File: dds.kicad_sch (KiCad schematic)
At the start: 23 parts, among them J2 Conn_01x01_Pin, U4 AD8014ARZ, U6 AD9834, Y1 ASE-xxxMHz

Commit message: draf 1 for sims
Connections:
- net Signal renamed SIGNAL
- net reset renamed RESET
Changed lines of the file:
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@@
 		)
 	)
-	(global_label "Signal"
+	(label "MCLK"
+		(at 106.68 120.65 180)
+		(effects
+			(font
+				(size 1.27 1.27)
+			)
+			(justify right bottom)
+		)
+	)
+	(label "MCLK"
+		(at 168.91 77.47 0)
+		(effects
+			(font
+				(size 1.27 1.27)
+			)
+			(justify left bottom)
+		)
+	)
+	(hierarchical_label "FSYNC"
+		(shape input)
+		(at 106.68 105.41 180)
+		(effects
+			(font
+				(size 1.27 1.27)
+			)
+			(justify right)
+		)
+	)
+	(hierarchical_label "RESET"
+		(shape input)
+		(at 106.68 107.95 180)
+		(effects
+			(font
+				(size 1.27 1.27)
+			)
+			(justify right)
+		)
+	)
+	(hierarchical_label "SCLK"
+		(shape input)
+		(at 106.68 100.33 180)
+		(effects
+			(font
+				(size 1.27 1.27)
+			)
+			(justify right)
+		)
+	)
+	(hierarchical_label "SDATA"
+		(shape input)
+		(at 106.68 102.87 180)
+		(effects
+			(font
+				(size 1.27 1.27)
+			)
+			(justify right)
+		)
+	)
+	(hierarchical_label "SIGNAL"
 		(shape input)
 		(at 266.7 118.11 0)
-		(fields_autoplaced yes)
 		(effects
 			(font
@@
 			(justify left)
 		)
-		(property "Intersheetrefs" "${INTERSHEET_REFS}"
-			(at 275.6117 118.11 0)
-			(effects
-				(font
-					(size 1.27 1.27)
-				)
-				(justify left)
-				(hide yes)
-			)
-		)
 	)
-	(global_label "reset"
-		(shape input)
-		(at 106.68 107.95 180)
-		(fields_autoplaced yes)
-		(effects
-			(font
-				(size 1.27 1.27)
-			)
-			(justify right)
-		)
-		(property "Intersheetrefs" "${INTERSHEET_REFS}"
-			(at 98.9776 107.95 0)
-			(effects
-				(font
-					(size 1.27 1.27)
-				)
-				(justify right)
-				(hide yes)
-			)
-		)
-	)
-	(global_label "SDATA"
-		(shape input)
-		(at 106.68 102.87 180)
-		(fields_autoplaced yes)
-		(effects
-			(font
-				(size 1.27 1.27)
-			)
-			(justify right)
-		)
-		(property "Intersheetrefs" "${INTERSHEET_REFS}"
-			(at 98.0705 102.87 0)
-			(effects
-				(font
-					(size 1.27 1.27)
-				)
-				(justify right)
-				(hide yes)
-			)
-		)
-	)
-	(global_label "MCLK"
-		(shape input)
-		(at 168.91 77.47 0)
-		(fields_autoplaced yes)
-		(effects
-			(font
-				(size 1.27 1.27)
-			)
-			(justify left)
-		)
-		(property "Intersheetrefs" "${INTERSHEET_REFS}"
-			(at 176.9147 77.47 0)
-			(effects
-				(font
-					(size 1.27 1.27)
-				)
-				(justify left)
-				(hide yes)
-			)
-		)
-	)
-	(global_label "FSYNC"
-		(shape input)
-		(at 106.68 105.41 180)
-		(fields_autoplaced yes)
-		(effects
-			(font
-				(size 1.27 1.27)
-			)
-			(justify right)
-		)
-		(property "Intersheetrefs" "${INTERSHEET_REFS}"
-			(at 97.7076 105.41 0)
-			(effects
-				(font
-					(size 1.27 1.27)
-				)
-				(justify right)
-				(hide yes)
-			)
-		)
-	)
-	(global_label "SCLK"
-		(shape input)
-		(at 106.68 100.33 180)
-		(fields_autoplaced yes)
-		(effects
-			(font
-				(size 1.27 1.27)
-			)
-			(justify right)
-		)
-		(property "Intersheetrefs" "${INTERSHEET_REFS}"
-			(at 98.9172 100.33 0)
-			(effects
-				(font
-					(size 1.27 1.27)
-				)
-				(justify right)
-				(hide yes)
-			)
-		)
-	)
-	(global_label "MCLK"
-		(shape input)
-		(at 106.68 120.65 180)
-		(fields_autoplaced yes)
-		(effects
-			(font
-				(size 1.27 1.27)
-			)
-			(justify right)
-		)
-		(property "Intersheetrefs" "${INTERSHEET_REFS}"
-			(at 98.6753 120.65 0)
-			(effects
-				(font
-					(size 1.27 1.27)
-				)
-				(justify right)
-				(hide yes)
-			)
-		)
-	)

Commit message: current routing stage
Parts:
- C1, C2, C3, C4, C5, C6, C7, C8, C9: footprint (none) -> Capacitor_SMD:C_0805_2012Metric
- J2: footprint (none) -> TestPoint:TestPoint_Pad_1.5x1.5mm
- L1, L2: footprint (none) -> 0806_L:IND_LSQM_B201616_TAY
- R1, R2, R3, R4, R5, R6, R7, R8: footprint (none) -> Resistor_SMD:R_0805_2012Metric
- U4: footprint R_8_ADI -> 1_High-speed analog interface:R_8_ADI
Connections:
- net +3V3 renamed +3.3V

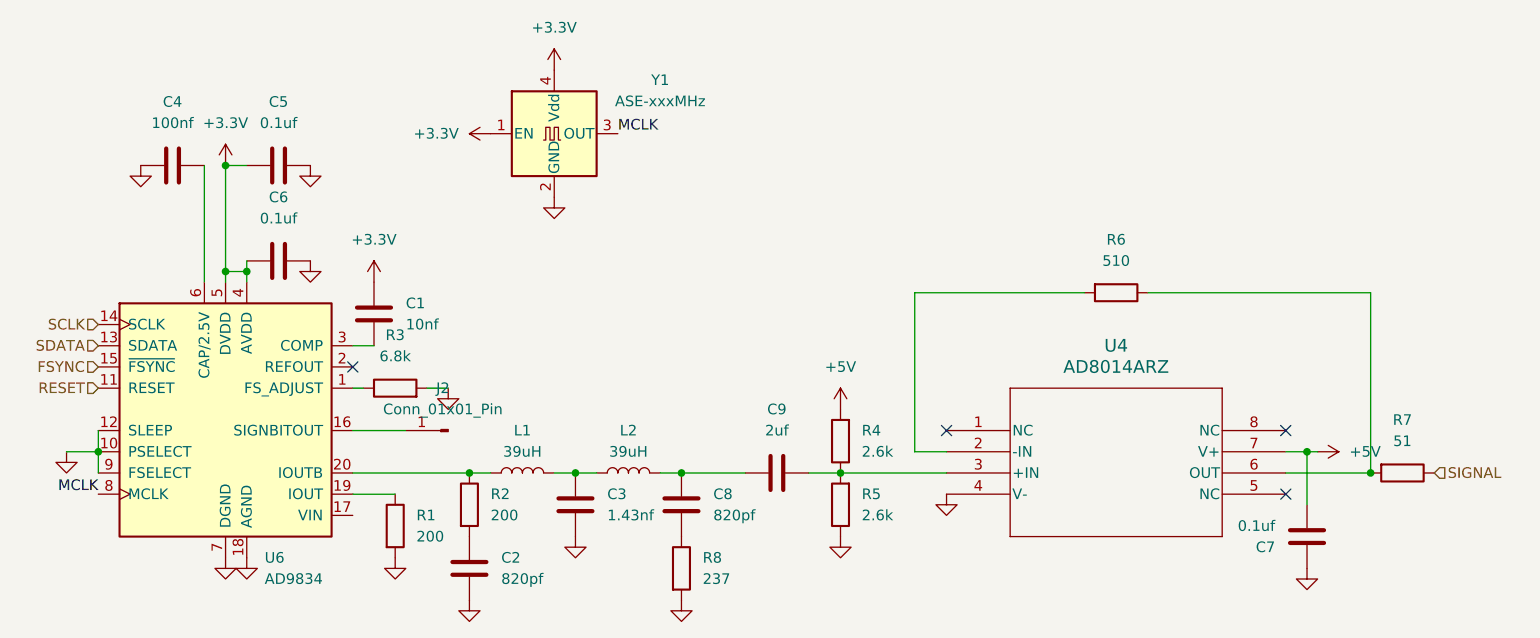
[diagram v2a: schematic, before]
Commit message: sim the new lpf
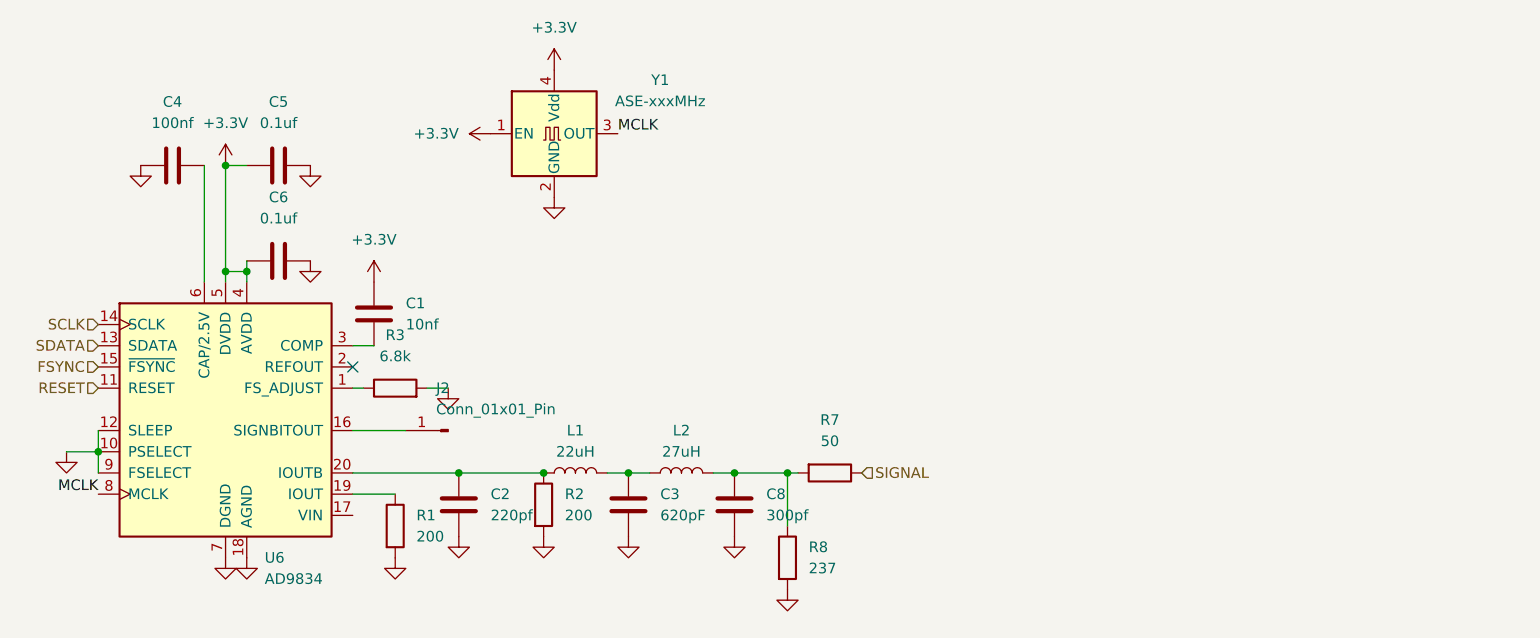
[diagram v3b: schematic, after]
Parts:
- removed C7: 0.1uf, Capacitor_SMD:C_0805_2012Metric, symbol Device:C
- removed C9: 2uf, Capacitor_SMD:C_0805_2012Metric, symbol Device:C
- removed R4, R5: 2.6k, Resistor_SMD:R_0805_2012Metric, symbol Device:R
- removed R6: 510, Resistor_SMD:R_0805_2012Metric, symbol Device:R
- removed U4: AD8014ARZ, 1_High-speed analog interface:R_8_ADI, symbol 1_High-speed analog interface:AD8014ARZ
- C1, C4, C5, C6: footprint Capacitor_SMD:C_0805_2012Metric -> Capacitor_SMD:C_0201_0603Metric
- C2: value 820pf -> 220pf; footprint Capacitor_SMD:C_0805_2012Metric -> Capacitor_SMD:C_0201_0603Metric
- C3: value 1.43nf -> 620pF; footprint Capacitor_SMD:C_0805_2012Metric -> Capacitor_SMD:C_0201_0603Metric
- C8: value 820pf -> 300pf; footprint Capacitor_SMD:C_0805_2012Metric -> Capacitor_SMD:C_0201_0603Metric
- L1: value 39uH -> 22uH
- L2: value 39uH -> 27uH
- R1, R2, R3, R8: footprint Resistor_SMD:R_0805_2012Metric -> Resistor_SMD:R_0201_0603Metric
- R7: value 51 -> 50; footprint Resistor_SMD:R_0805_2012Metric -> Resistor_SMD:R_0201_0603Metric
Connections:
- net GND: now also C8.1, R2.2
- net at R7.2: now also C8.2, L2.2, R8.1
- net at C2.2: now also L1.1, R2.1, U6.20 (IOUTB); no longer R2.2
- no-connect marks 4 -> 1
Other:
- moved on the sheet: C2, C3, C8, L1, L2, R2, R7, R8
